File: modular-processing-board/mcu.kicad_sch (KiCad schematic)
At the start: 41 parts, among them J201 Conn_02x06_Counter_Clockwise, SW701 SW_Push, U201 STM32H723ZGTx, Y1201 25MHz

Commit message: decided on fully differential configuratinon with ths4521 for both ADC inputs
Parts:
- removed C216, C217: 0.1uF, Capacitor_SMD:C_0201_0603Metric, symbol Device:C_Small
- added U202, U203: THS4521IDGK, Package_SO:VSSOP-8_3x3mm_P0.65mm, symbol Amplifier_Difference:THS4521IDGK
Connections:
- net MCU_ADC12 is gone; now on net SDRAM.~{CS0}: U201.44 (PC4)
- net SDRAM.~{CKE0}: now also U201.45 (PC5); no longer U201.29 (PC3_C)
- net SDRAM.~{CS0}: no longer U201.28 (PC2_C)
- net MCU_ADC12_INTERLEAVED_INN5: now reaches U201.46 (PB0)
- net MCU_ADC12_INTERLEAVED_INP5: now reaches U201.47 (PB1)
- new net MCU_ADC3_DIRECT_INN0: U201.28 (PC2_C)
- new net MCU_ADC3_DIRECT_INP0: U201.29 (PC3_C)
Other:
- note added: "ADC12 IN"
- note added: "PB1: fast channel (fastest for ADC1,2)"
- note added: "PC2_C, P3_C: direct channels (fastest for ADC3)"
- note removed: "VCAP"
- moved on the sheet: C1227, C201, C202, C203, C204, C205, C206, C207, C208, C209, C210, C211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

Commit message: Finished basic HW (next) Fix-up all labeling, then start laying out
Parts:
- removed L201: GZ2012D101TF, Inductor_SMD:L_0805_2012Metric, symbol Device:L_Small
- removed R206: 10k, Resistor_SMD:R_0603_1608Metric, symbol Device:R_Small
- removed U202, U203: THS4521IDGK, Package_SO:VSSOP-8_3x3mm_P0.65mm, symbol Amplifier_Difference:THS4521IDGK
- added C216: 0.1uF, Capacitor_SMD:C_0201_0603Metric, symbol Device:C_Small
- added R207: 10k, Resistor_SMD:R_0603_1608Metric, symbol Device:R_Small
- added R208: 470, Resistor_SMD:R_0402_1005Metric, symbol Device:R_Small
- added SW201: SW_Push, iw-misc:SW_TS-1088-AR02016, symbol Switch:SW_Push
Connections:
- net +3V3: now also R207.1
- net GND: now also J201.6 (Pin_6), C216.2, R208.2
- net MCU_BOOT0: now also J201.5 (Pin_5), C216.1, R207.2, SW201.1
- net MCU_VREF: no longer J201.6 (Pin_6)
- net USB_SENSE: now also U201.9 (PC15)
- net PWM.0_HI: now reaches U201.18 (PF6)
- net ADC_ALERT: now reaches U201.2 (PE3)
- net PWM.0_LI: now reaches U201.20 (PF8)
- net PWM.1_LI: now reaches U201.21 (PF9)
- net SDMMC.CMD: now reaches U201.34 (PA0)
- net I2C.SCL: now reaches U201.69 (PB10)
- net PBOOST_EN: now reaches U201.7 (PC13)
- net I2C.SDA: now reaches U201.70 (PB11)
- net PSEPIC_EN: now reaches U201.8 (PC14)
- net MCU_ADC12_INTERLEAVED_INN5 renamed MCU_ADC12_FAST_INN5
- net MCU_ADC12_INTERLEAVED_INP5 renamed MCU_ADC12_FAST_INP5
- net MCU_ADC3 renamed PWM.1_HI
- new net: R208.1, SW201.2
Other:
- note removed: "ADC12 IN"
- moved on the sheet: C1227, C201, C213, C214, C215, C220, C221, C223, C708, J201, R1201, R1203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

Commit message: completed schematic
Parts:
- added C217: 0.1uF, Capacitor_SMD:C_0201_0603Metric, symbol Device:C_Small
- added D201, D401: RED, LED_SMD:LED_0603_1608Metric, symbol Device:LED_Small
- added R206, R209: 1k, Resistor_SMD:R_0402_1005Metric, symbol Device:R_Small
- added R210: 470, Resistor_SMD:R_0402_1005Metric, symbol Device:R_Small
- added R211: 0, Resistor_SMD:R_0805_2012Metric_Pad1.20x1.40mm_HandSolder, symbol Device:R_Small
- added R212, R213: 47, Resistor_SMD:R_0603_1608Metric, symbol Device:R_Small
- added SW602: SW_Push, iw-misc:SW_TS-1088-AR02016, symbol Switch:SW_Push
- R201: value 0 -> 4.7k; footprint Resistor_SMD:R_0805_2012Metric_Pad1.20x1.40mm_HandSolder -> Resistor_SMD:R_0402_1005Metric; LCSC Part Number C17477 -> C25900; Manufacturing Part Number 0805W8F0000T5E -> 0402WGF4701TCE
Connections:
- net VREF_MCU is gone; now on net VDDA: C218.1, C219.1
- net +3V3: no longer C214.1, C215.1, R201.2
- net GND: now also J201.8 (Pin_8), C217.2, R206.1, R209.1, R210.2; no longer J201.10 (Pin_10), J201.9 (Pin_9)
- net VDDA: now also C214.1, C215.1, U201.33 (VDDA), R211.2
- net LED_2: now reaches U201.118 (PD4)
- net LED_2: now also D401.2 (A)
- net LED_1: now reaches U201.119 (PD5)
- net LED_1: now also D201.2 (A)
- net BUTTON_1: now reaches U201.123 (PD7)
- net BUTTON_1: now also R201.2, C217.1, SW602.1
- net VCORE_3V3: now reaches R201.1
- net VCORE_3V3: no longer U201.33 (VDDA)
- net UART5_RX: now reaches U201.73 (PB12)
- net UART5_RX: now also R213.1
- net UART5_TX: now reaches U201.74 (PB13)
- net UART5_TX: now also R212.1
- net MCU_VREF: no longer names the net of U201.32 (VREF+)
- net MCU_VREF: now also R211.1
- new net: D201.1 (K), R206.2
- new net: J201.9 (Pin_9), R213.2
- new net: D401.1 (K), R209.2
- new net: R210.1, SW602.2
- new net: J201.10 (Pin_10), R212.2
- no-connect marks 0 -> 21
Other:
- note added: "MCU"
- moved on the sheet: C202, C203, C204, C205, C206, C207, C208, C209, C210, C211, C212, C213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

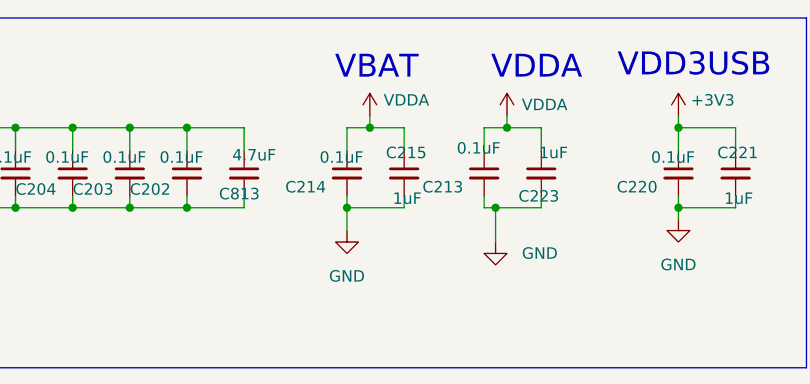
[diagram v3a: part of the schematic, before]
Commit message: various changes to schematic (next) add bias resistors after testing results on acoustic-carrier-board
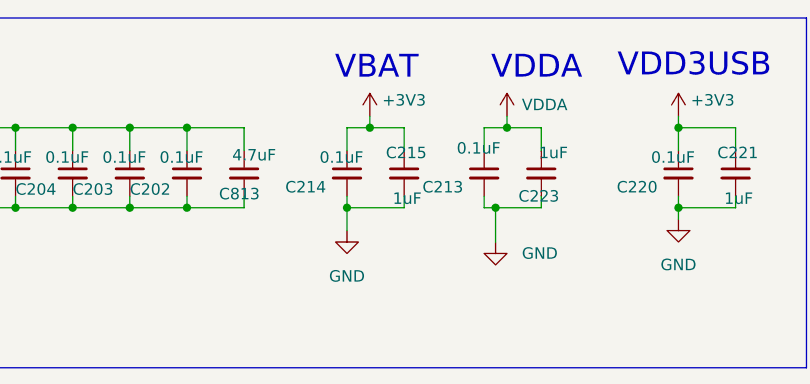
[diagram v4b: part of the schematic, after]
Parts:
- C202, C203, C204, C205, C206, C207, C208, C209, C210, C211, C212, C213, C214, C216, C217, C218, C220, C222, C224, C708: footprint Capacitor_SMD:C_0201_0603Metric -> Capacitor_SMD:C_0402_1005Metric; LPN (none) -> C307331; MPN (none) -> CL05B104KB54PNC
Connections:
- net +3V3: now also C214.1, C215.1
- net VDDA: no longer C214.1, C215.1

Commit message: started layout
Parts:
- removed C216: 0.1uF, Capacitor_SMD:C_0402_1005Metric, symbol Device:C_Small
- removed R207: 10k, Resistor_SMD:R_0603_1608Metric, symbol Device:R_Small
- removed R208: 470, Resistor_SMD:R_0402_1005Metric, symbol Device:R_Small
- removed SW201: SW_Push, iw-misc:SW_TS-1088-AR02016, symbol Switch:SW_Push

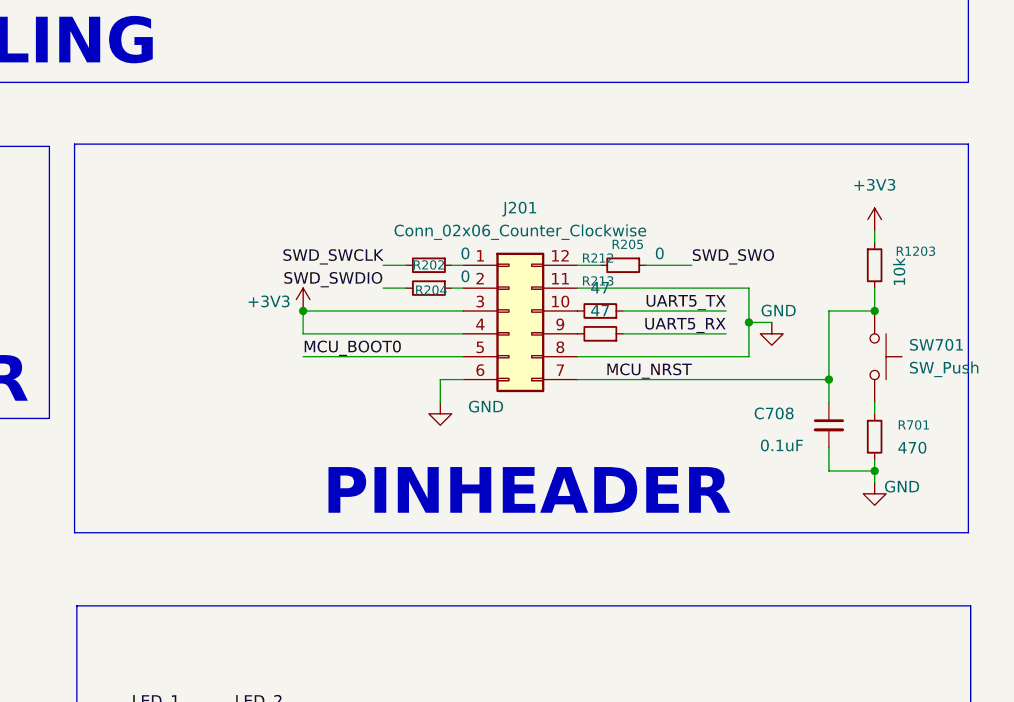
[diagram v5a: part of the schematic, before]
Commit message: removed power input jumpers to single one, added trace impedances and production restrictions (next) route sdram
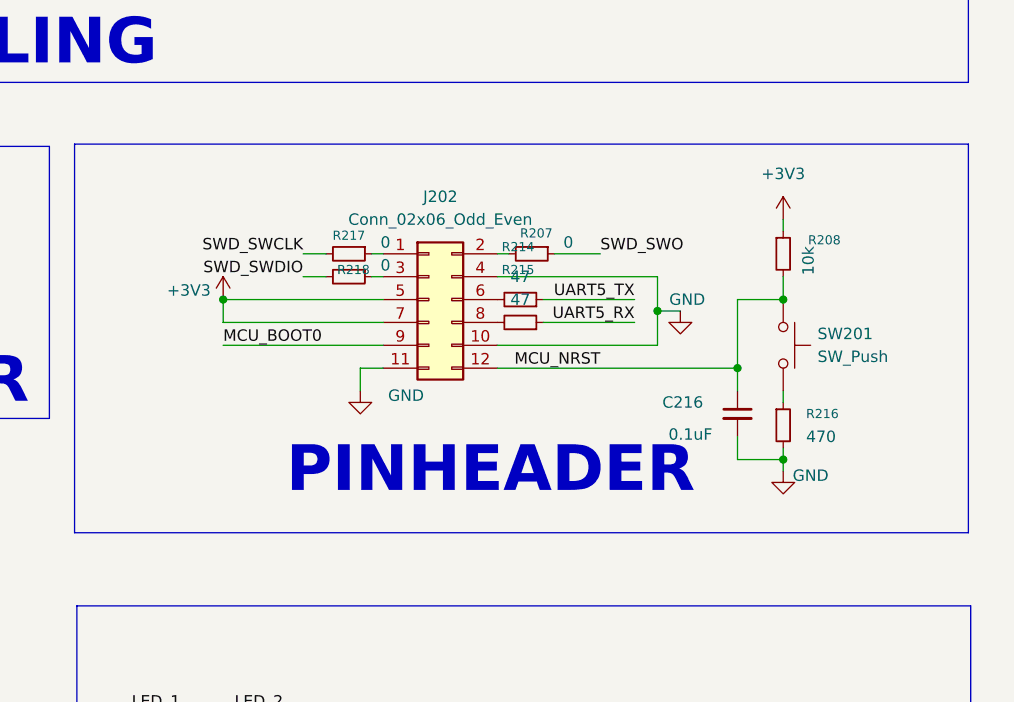
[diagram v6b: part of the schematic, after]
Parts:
- removed C708: 0.1uF, Capacitor_SMD:C_0402_1005Metric, symbol Device:C_Small
- removed J201: Conn_02x06_Counter_Clockwise, Connector_PinHeader_1.00mm:PinHeader_2x06_P1.00mm_Vertical, symbol Connector_Generic:Conn_02x06_Counter_Clockwise
- removed R1203: 10k, Resistor_SMD:R_0603_1608Metric, symbol Device:R_Small
- removed R202, R204, R205: 0, Resistor_SMD:R_0805_2012Metric_Pad1.20x1.40mm_HandSolder, symbol Device:R_Small
- removed R212, R213: 47, Resistor_SMD:R_0603_1608Metric, symbol Device:R_Small
- removed R701: 470, Resistor_SMD:R_0402_1005Metric, symbol Device:R_Small
- removed SW701: SW_Push, iw-misc:SW_TS-1088-AR02016, symbol Switch:SW_Push
- added C216: 0.1uF, Capacitor_SMD:C_0402_1005Metric, symbol Device:C_Small
- added J202: Conn_02x06_Odd_Even, Connector_PinHeader_2.54mm:PinHeader_2x06_P2.54mm_Vertical, symbol Connector_Generic:Conn_02x06_Odd_Even
- added R207, R217, R218: 0, Resistor_SMD:R_0805_2012Metric_Pad1.20x1.40mm_HandSolder, symbol Device:R_Small
- added R208: 10k, Resistor_SMD:R_0603_1608Metric, symbol Device:R_Small
- added R214, R215: 47, Resistor_SMD:R_0603_1608Metric, symbol Device:R_Small
- added R216: 470, Resistor_SMD:R_0402_1005Metric, symbol Device:R_Small
- added SW201: SW_Push, iw-misc:SW_TS-1088-AR02016, symbol Switch:SW_Push
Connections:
- net +3V3: now also J202.5 (Pin_5), J202.7 (Pin_7), R208.1
- net GND: now also C216.2, J202.10 (Pin_10), J202.11 (Pin_11), J202.4 (Pin_4), R216.2
- net MCU_BOOT0: now also J202.9 (Pin_9)
- net MCU_NRST: now also C216.1, J202.12 (Pin_12), R208.2, SW201.1
- net SWD_SWCLK: now also R217.2
- net SWD_SWDIO: now also R218.2
- net SWD_SWO: now also R207.1
- net UART5_RX: now also R215.1
- net UART5_TX: now also R214.1
- new net: J202.8 (Pin_8), R215.2
- new net: J202.3 (Pin_3), R218.1
- new net: R216.1, SW201.2
- new net: J202.2 (Pin_2), R207.2
- new net: J202.1 (Pin_1), R217.1
- new net: J202.6 (Pin_6), R214.2

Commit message: rough length mamatching for sdram (next) route PSSI-bus
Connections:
- net PSSI.D2: now also U201.125 (PG10); no longer U201.98 (PC8)

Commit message: replaced sdmmc connector, added smmc trace, added u.fl. connectors
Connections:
- net VCORE_3V3 is gone; now on net +3V3: R201.1
- net SDMMC.CD: now reaches U201.35 (PA1)
- net USB_DM renamed USB_DN
- no-connect marks 21 -> 20
